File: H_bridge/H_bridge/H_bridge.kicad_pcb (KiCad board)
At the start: 2 copper layers, 49.8 x 36 mm, 17 parts, among them J1 Screw_Terminal_01x02, J2 Screw_Terminal_01x06, J3 Pins_02x10_P1.27mm_TH, U1 VNH7040AYTR

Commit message: puente H, Done
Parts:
- added C2: 470uF, Capacitor_SMD:CP_Elec_10x14.3, F.Cu at (146.2, 68.5)
- added C4: 100nF, PCM_Capacitor_SMD_AKL:C_0805_2012Metric, F.Cu at (139.5, 73.8)
- U1: footprint UL_Hbridge:POWERSSO-36TP_STM-M -> UL_Full_H_Bridge_SMD:POWERSSO-36TP_STM-M
- moved R2 25.3 mm to (126.0, 76.7), turned to 90 degrees
- moved R1 15.8 mm to (124.2, 76.5)
- moved R4 12.7 mm to (137.2, 58.2), turned to -90 degrees
- moved R6 7.00 mm to (133.8, 58.2)
- moved U1 6.43 mm to (133.0, 67.0)
- moved R3 5.89 mm to (136.5, 75.0), turned to 0 degrees
- moved R7 4.59 mm to (139.0, 58.2)
- moved R5 4.03 mm to (135.5, 58.2)
- moved C1 3.61 mm to (140.8, 58.2)
- moved J1 2.86 mm to (141.2, 81.2)
- moved R8 2.30 mm to (143.0, 60.5), turned to -90 degrees
- moved J3 0.50 mm to (117.0, 56.2)
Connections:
- J3 pad 14: Net-(C1-Pad1) -> Net-(J3-Pad14)
- J3 pad 8: Net-(J3-Pad8) -> Net-(C1-Pad1)
- R1 pad 2: /INA -> /SEL0
- R2 pad 2: /INB -> /INA
- R4 pad 1: Net-(J3-Pad8) -> Net-(J3-Pad10)
- R4 pad 2: /SEL0 -> /CS/DF_EN
- R5 pad 1: Net-(J3-Pad10) -> Net-(J3-Pad12)
- R5 pad 2: /SEL1 -> /INB
- R6 pad 1: Net-(J3-Pad12) -> Net-(J3-Pad14)
- R6 pad 2: /CS/DF_EN -> /SEL1
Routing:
- net /Drain_Low_SideA: track 36.8 -> 113.7 mm
- net +24V: track 12.7 -> 47.3 mm
- net Net-(C1-Pad1): track 47.4 -> 24.9 mm, vias 1 -> 0
- net Net-(J3-Pad14): track 0.00 -> 21.8 mm
- net Net-(J3-Pad8): track 20.5 -> 0.00 mm
- net Net-(J3-Pad12): track 36.6 -> 21.2 mm, vias 1 -> 0
- net Net-(J3-Pad2): track 39.0 -> 24.7 mm
- net /SEL1: track 17.3 -> 3.95 mm
- net /INA: track 3.72 -> 12.8 mm
- net /SEL0: track 4.97 -> 13.8 mm
- net Net-(J3-Pad6): track 25.8 -> 31.9 mm, vias 0 -> 1
- net Net-(J3-Pad10): track 26.1 -> 22.2 mm
- net /CS/DF: track 7.11 -> 8.78 mm
- net Net-(J3-Pad4): track 20.5 -> 22.1 mm, vias 0 -> 1
- net /Drain_Low_SideB: track 39.7 -> 38.1 mm, vias 1 -> 0
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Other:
- board text added: "*"

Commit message: avances pcb
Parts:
- moved H1 55.8 mm to (184.2, 92.8)
- moved H4 55.6 mm to (185.8, 49.8)
- moved H3 37.0 mm to (185.2, 79.8)
- moved H2 29.5 mm to (177.8, 53.8)
- moved R6 18.8 mm to (152.2, 61.5), turned to 180 degrees
- moved C1 18.4 mm to (130.8, 73.8)
- moved R5 17.5 mm to (152.2, 63.2), turned to 180 degrees
- moved R7 16.8 mm to (152.2, 68.5), turned to 180 degrees
- moved R4 16.4 mm to (152.2, 65.0), turned to 180 degrees
- moved R1 14.0 mm to (128.8, 63.2), turned to 0 degrees
- moved R2 11.7 mm to (128.8, 65.2), turned to 0 degrees
- moved R8 11.2 mm to (152.2, 66.8), turned to 180 degrees
- moved R3 11.0 mm to (128.8, 67.2)
- moved C2 7.85 mm to (150.2, 75.2), turned to 0 degrees
- moved J1 7.31 mm to (140.5, 74.0)
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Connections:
- U1 pad 37: Heatsink -> +24V
- U1 pad 38: Heatsink -> /Drain_Low_SideA
- U1 pad 39: Heatsink -> /Drain_Low_SideB
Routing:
- net /Drain_Low_SideA: track 113.7 -> 0.00 mm
- net +24V: track 47.3 -> 0.00 mm, vias 1 -> 0
- net /Drain_Low_SideB: track 38.1 -> 0.00 mm
- net Net-(J3-Pad6): track 31.9 -> 0.00 mm, vias 1 -> 0
- net Net-(C1-Pad1): track 24.9 -> 0.00 mm
- net Net-(J3-Pad2): track 24.7 -> 0.00 mm, vias 1 -> 0
- net Net-(J3-Pad10): track 22.2 -> 0.00 mm
- net Net-(J3-Pad4): track 22.1 -> 0.00 mm, vias 1 -> 0
- net Net-(J3-Pad14): track 21.8 -> 0.00 mm
- net Net-(J3-Pad12): track 21.2 -> 0.00 mm
- net /SEL0: track 13.8 -> 0.00 mm
- net /INA: track 12.8 -> 0.00 mm
- net /CS/DF: track 8.78 -> 0.00 mm
- net /SEL1: track 3.95 -> 0.00 mm
- net /PWM: track 3.44 -> 0.00 mm
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- removed copper zone on B.Cu, net GND
- removed copper zone on F.Cu, net GND
- removed copper zone on F.Cu, net Heatsink
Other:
- copper layers 2 -> 4

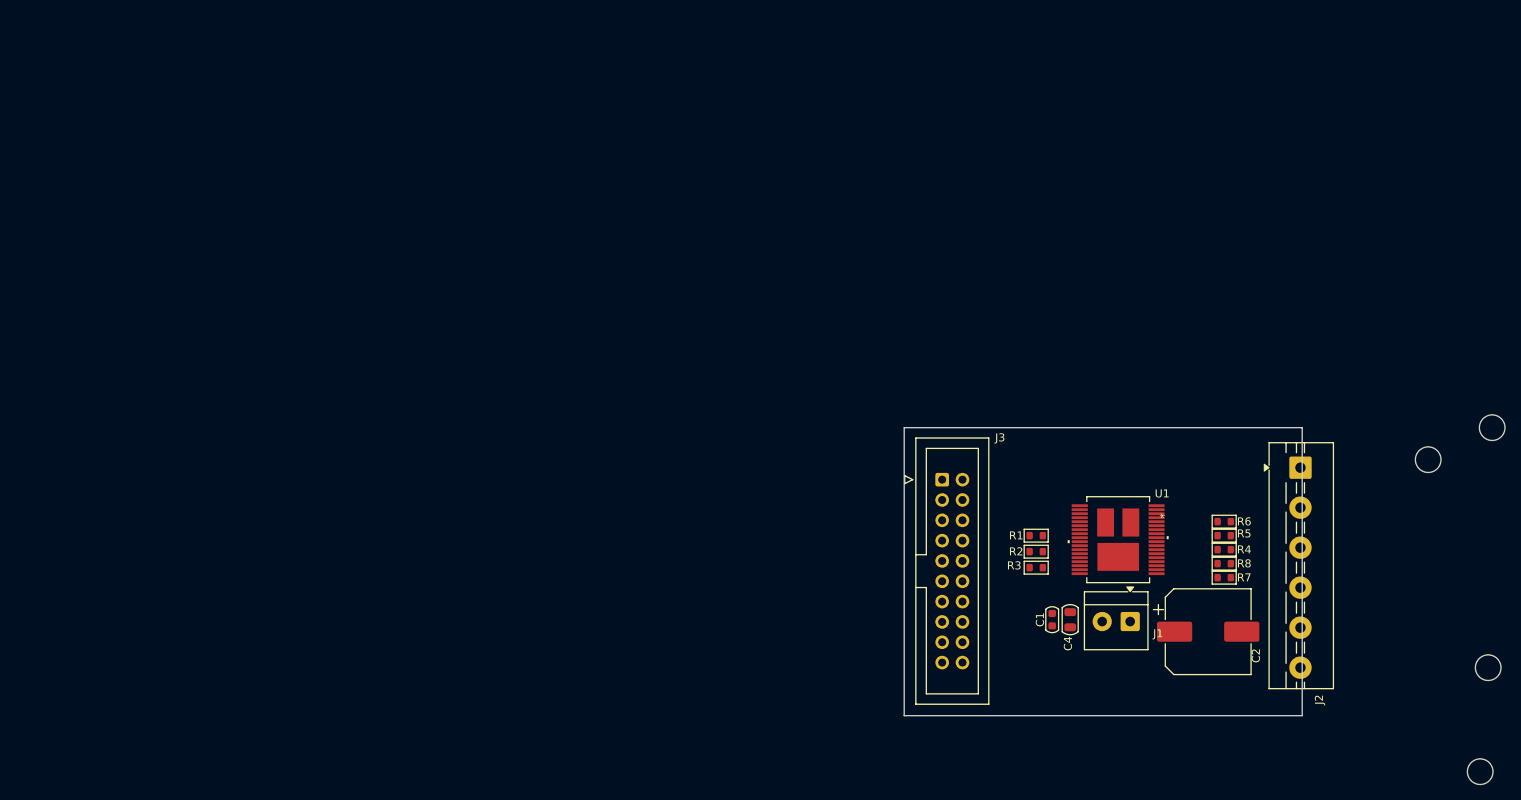
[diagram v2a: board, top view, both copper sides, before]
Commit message: Puente H Done
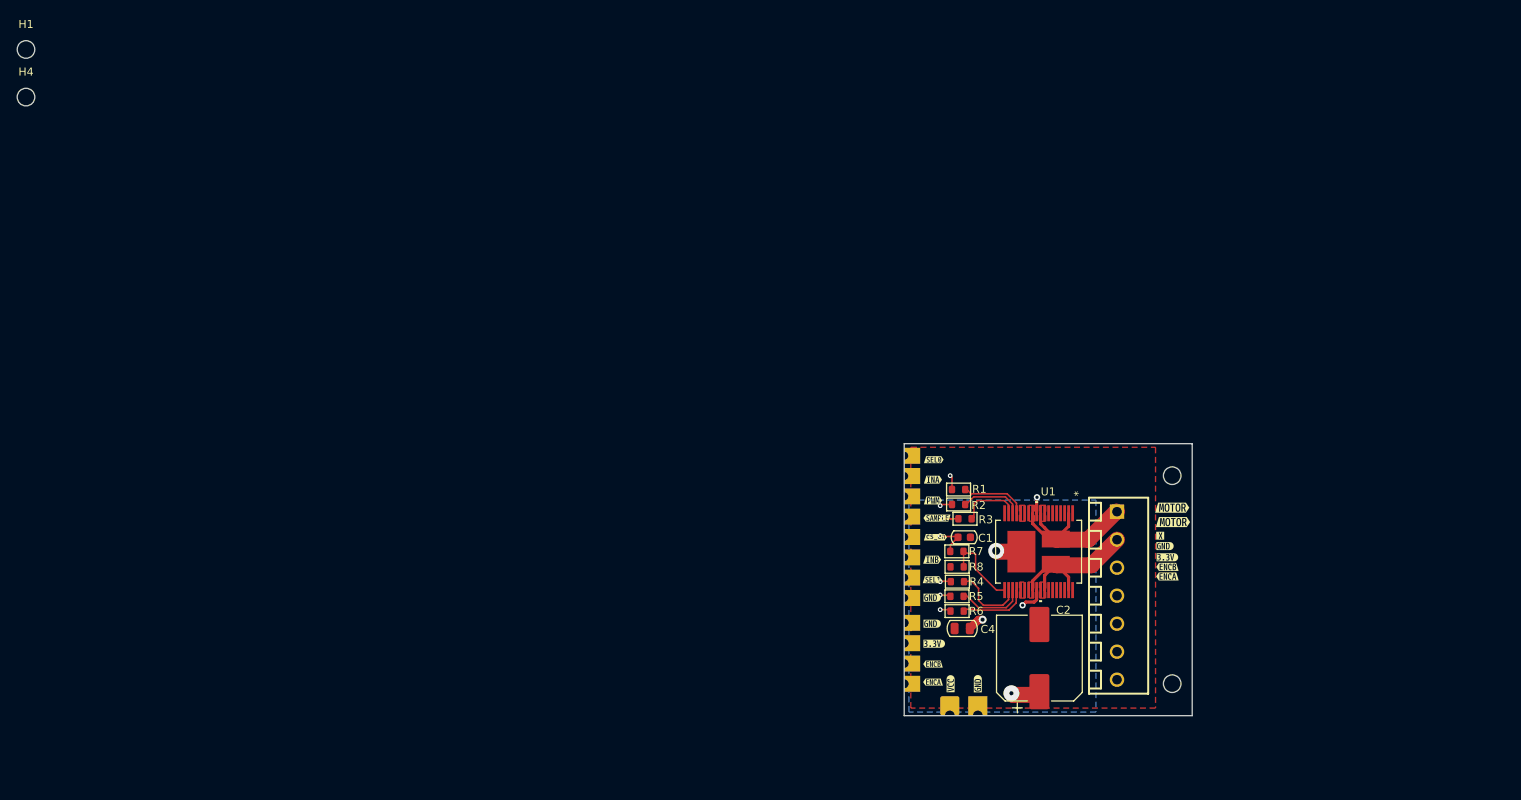
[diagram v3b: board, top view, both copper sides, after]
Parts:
- removed J1: Screw_Terminal_01x02, TerminalBlock_4Ucon:TerminalBlock_4Ucon_1x02_P3.50mm_Horizontal
- removed J3: Pins_02x10_P1.27mm_TH, Connector_IDC:IDC-Header_2x10_P2.54mm_Vertical
- added P1: Header-Female-2.54_1x8, EasyEDA:HDR-TH_8P-P2.54-V-F_2, B.Cu at (112.2, 62.1)
- added U2: HX PZ2.54-1X4P ZZ, EasyEDA:HDR-TH_4P-P2.54-V-M, F.Cu at (112.2, 78.0)
- added U4: DB125-3.5-7P-GN-S, EasyEDA:CONN-TH_7P-P3.50_DORABO_DB125-3.5-7P-GN-S, F.Cu at (138.8, 70.8)
- added kibuzzard-6918ABEE: G***, kibuzzard-6918ABEE, F.Cu at (144.8, 64.5)
- added kibuzzard-6918ABEE: G***, kibuzzard-6918ABEE, F.Cu at (115.8, 71.0)
- added kibuzzard-6918ABEE: G***, kibuzzard-6918ABEE, F.Cu at (121.5, 81.8)
- added kibuzzard-6918ABEE: G***, kibuzzard-6918ABEE, F.Cu at (115.8, 74.2)
- added kibuzzard-6918ABFE: G***, kibuzzard-6918ABFE, F.Cu at (116.0, 76.8)
- added kibuzzard-6918ABFE: G***, kibuzzard-6918ABFE, F.Cu at (145.2, 66.0)
- added kibuzzard-6918AC69: G***, kibuzzard-6918AC69, F.Cu at (145.2, 68.3)
- added kibuzzard-6918AC7D: G***, kibuzzard-6918AC7D, F.Cu at (145.2, 67.2)
- added kibuzzard-6918AEC8: G***, kibuzzard-6918AEC8, F.Cu at (115.8, 66.2)
- added kibuzzard-6918AF5D: G***, kibuzzard-6918AF5D, F.Cu at (115.8, 58.9)
- added kibuzzard-6918AF91: G***, kibuzzard-6918AF91, F.Cu at (115.8, 56.2)
- added kibuzzard-6918AF9A: G***, kibuzzard-6918AF9A, F.Cu at (116.0, 53.8)
- added kibuzzard-6918AFA7: G***, kibuzzard-6918AFA7, F.Cu at (116.2, 63.5)
- added kibuzzard-6918AFBB: G***, kibuzzard-6918AFBB, F.Cu at (115.8, 68.8)
- added kibuzzard-6918AFD3: G***, kibuzzard-6918AFD3, F.Cu at (116.3, 61.0)
- added kibuzzard-6918B00F: G***, kibuzzard-6918B00F, F.Cu at (145.8, 61.5)
- added kibuzzard-6918B00F: G***, kibuzzard-6918B00F, F.Cu at (145.8, 59.8)
- added kibuzzard-6918B09A: G***, kibuzzard-6918B09A, F.Cu at (144.2, 63.2)
- added kibuzzard-6918B0DE: G***, kibuzzard-6918B0DE, F.Cu at (115.8, 81.5)
- added kibuzzard-6918B0E8: G***, kibuzzard-6918B0E8, F.Cu at (115.8, 79.3)
- added kibuzzard-6918B0F5: G***, kibuzzard-6918B0F5, F.Cu at (118.0, 81.8)
- H1, H2, H3, H4: footprint MountingHole:MountingHole_3.2mm_M3 -> MountingHole:MountingHole_2.2mm_M2
- J2: value Screw_Terminal_01x06 -> Screw_Terminal_01x02; footprint TerminalBlock:TerminalBlock_MaiXu_MX126-5.0-06P_1x06_P5.00mm -> TerminalBlock_4Ucon:TerminalBlock_4Ucon_1x02_P3.50mm_Horizontal
- moved H1 203.0 mm to (2.48, 2.48), turned to 0 degrees
- moved H4 187.9 mm to (2.48, 8.43)
- moved J2 53.7 mm to (118.0, 85.7), turned to 0 degrees
- moved H3 39.6 mm to (145.8, 81.8)
- moved R6 35.2 mm to (118.9, 72.7), turned to 0 degrees
- moved R5 34.3 mm to (118.8, 70.8), turned to 0 degrees
- moved R4 33.6 mm to (118.9, 69.0), turned to 0 degrees
- moved R7 33.6 mm to (118.8, 65.2), turned to 0 degrees
- moved R8 33.4 mm to (118.9, 67.1), turned to 0 degrees
- moved H2 32.1 mm to (145.8, 55.8)
- moved C2 21.4 mm to (129.2, 78.5), turned to 90 degrees
- moved C1 15.1 mm to (119.8, 63.5), turned to 0 degrees
- moved C4 13.5 mm to (119.5, 74.8), turned to 180 degrees
- moved R2 11.4 mm to (119.0, 59.4)
- moved R1 11.3 mm to (119.0, 57.5)
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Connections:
- net Net-(C1-Pad1) renamed /SAMPLE
- J2 pad 1: /Drain_Low_SideA -> +24V
- J2 pad 2: /Drain_Low_SideB -> GND
- R1 pad 1: Net-(J3-Pad2) -> /selo
- R2 pad 1: Net-(J3-Pad4) -> /ina
- R3 pad 1: Net-(J3-Pad6) -> /pwm
- R4 pad 1: Net-(J3-Pad10) -> /cs/df_en
- R5 pad 1: Net-(J3-Pad12) -> /inb
- R6 pad 1: Net-(J3-Pad14) -> /sel1
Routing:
- net 3.3V: track 0.00 -> 27.6 mm
- net /ENC_B: track 0.00 -> 26.6 mm
- net /ENC_A: track 0.00 -> 26.2 mm
- net /Drain_Low_SideA: track 0.00 -> 22.0 mm
- net /Drain_Low_SideB: track 0.00 -> 21.6 mm
- net +24V: track 0.00 -> 14.3 mm, vias 0 -> 5
- net /SAMPLE: track 0.00 -> 11.5 mm, vias 0 -> 1
- net /inb: track 0.00 -> 10.2 mm, vias 0 -> 1
- net /CS/DF: track 0.00 -> 10.2 mm
- net /cs/df_en: track 0.00 -> 9.63 mm, vias 0 -> 1
- net /CS/DF_EN: track 0.00 -> 9.19 mm
- net /sel1: track 0.00 -> 8.91 mm, vias 0 -> 1
- net /SEL1: track 0.00 -> 8.78 mm
- net /ina: track 0.00 -> 8.62 mm, vias 0 -> 1
- net /selo: track 0.00 -> 8.61 mm, vias 0 -> 1
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- added copper zone on B.Cu, net +24V
- added copper zone on F.Cu, net /Drain_Low_SideA
- added copper zone on F.Cu, net /Drain_Low_SideB
- added copper zone on F.Cu, net GND
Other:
- board size 49.8 x 36 mm -> 36 x 34 mm

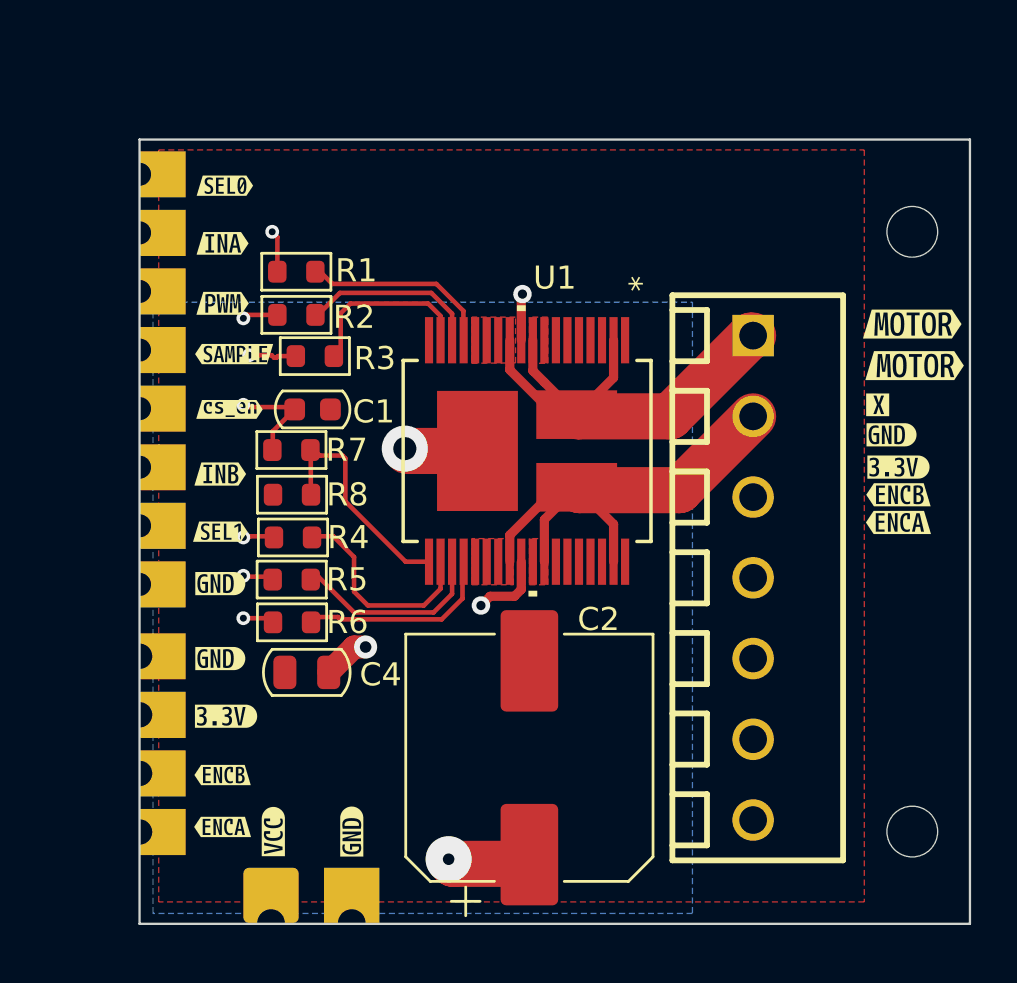
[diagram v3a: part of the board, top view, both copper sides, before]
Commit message: salidas motor castellated
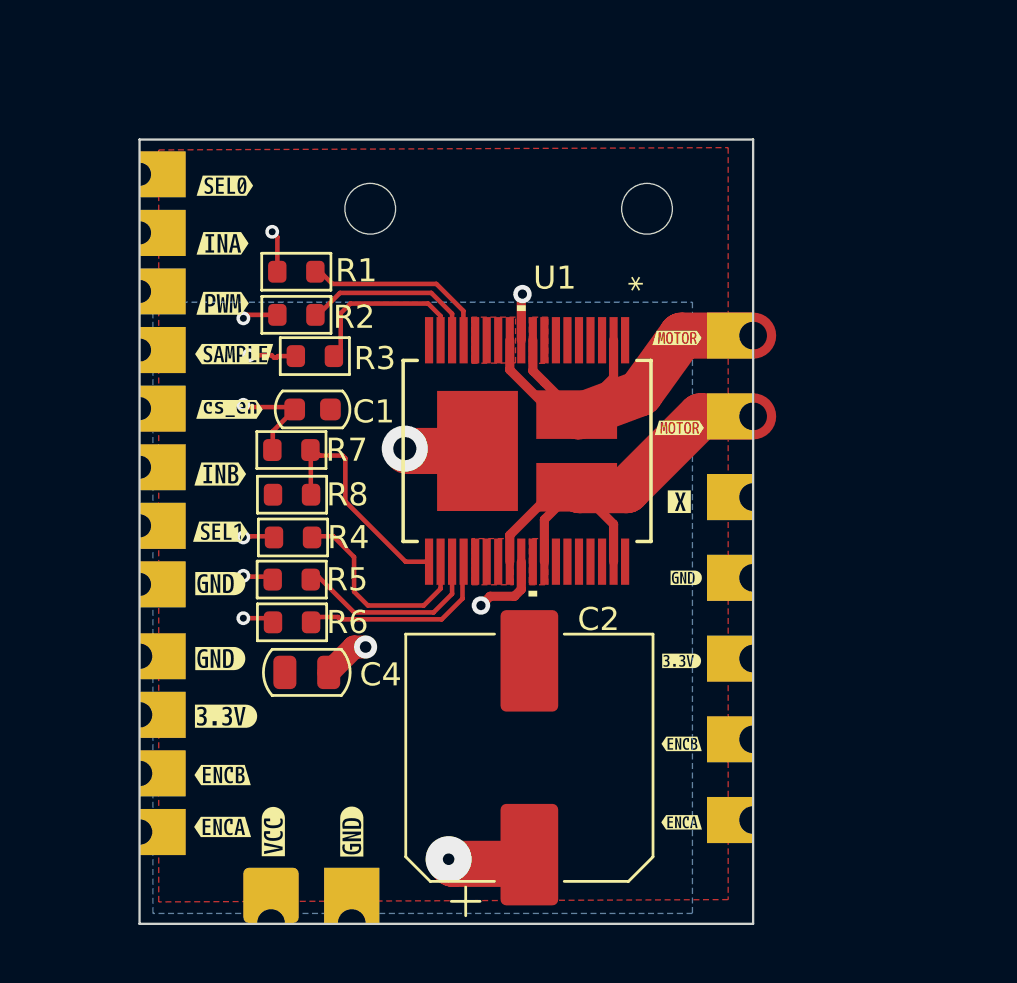
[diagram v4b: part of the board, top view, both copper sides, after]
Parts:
- removed the kibuzzard-6918ABEE at (144.8, 64.5)
- removed the kibuzzard-6918ABFE at (145.2, 66.0)
- removed kibuzzard-6918AC69: G***, kibuzzard-6918AC69
- removed kibuzzard-6918AC7D: G***, kibuzzard-6918AC7D
- removed kibuzzard-6918B00F (x2): G***, kibuzzard-6918B00F
- added kibuzzard-6918BF9B: G***, kibuzzard-6918BF9B, F.Cu at (135.7, 64.2)
- added kibuzzard-6918BF9B: G***, kibuzzard-6918BF9B, F.Cu at (135.6, 60.4)
- added kibuzzard-6918BFE8: G***, kibuzzard-6918BFE8, F.Cu at (135.9, 70.8)
- added kibuzzard-6918C0A7: G***, kibuzzard-6918C0A7, F.Cu at (135.8, 74.3)
- added kibuzzard-6918C0B5: G***, kibuzzard-6918C0B5, F.Cu at (135.8, 78.0)
- added kibuzzard-6918C0C9: G***, kibuzzard-6918C0C9, F.Cu at (135.8, 81.3)
- moved H3 29.3 mm to (134.2, 54.8)
- moved H2 23.5 mm to (122.2, 54.8)
- moved kibuzzard-6918B09A 9.57 mm to (135.7, 67.5)
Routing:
- net /ina: track 8.62 -> 9.23 mm
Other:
- board size 36 x 34 mm -> 26.6 x 34 mm
